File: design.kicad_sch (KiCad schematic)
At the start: 13 parts

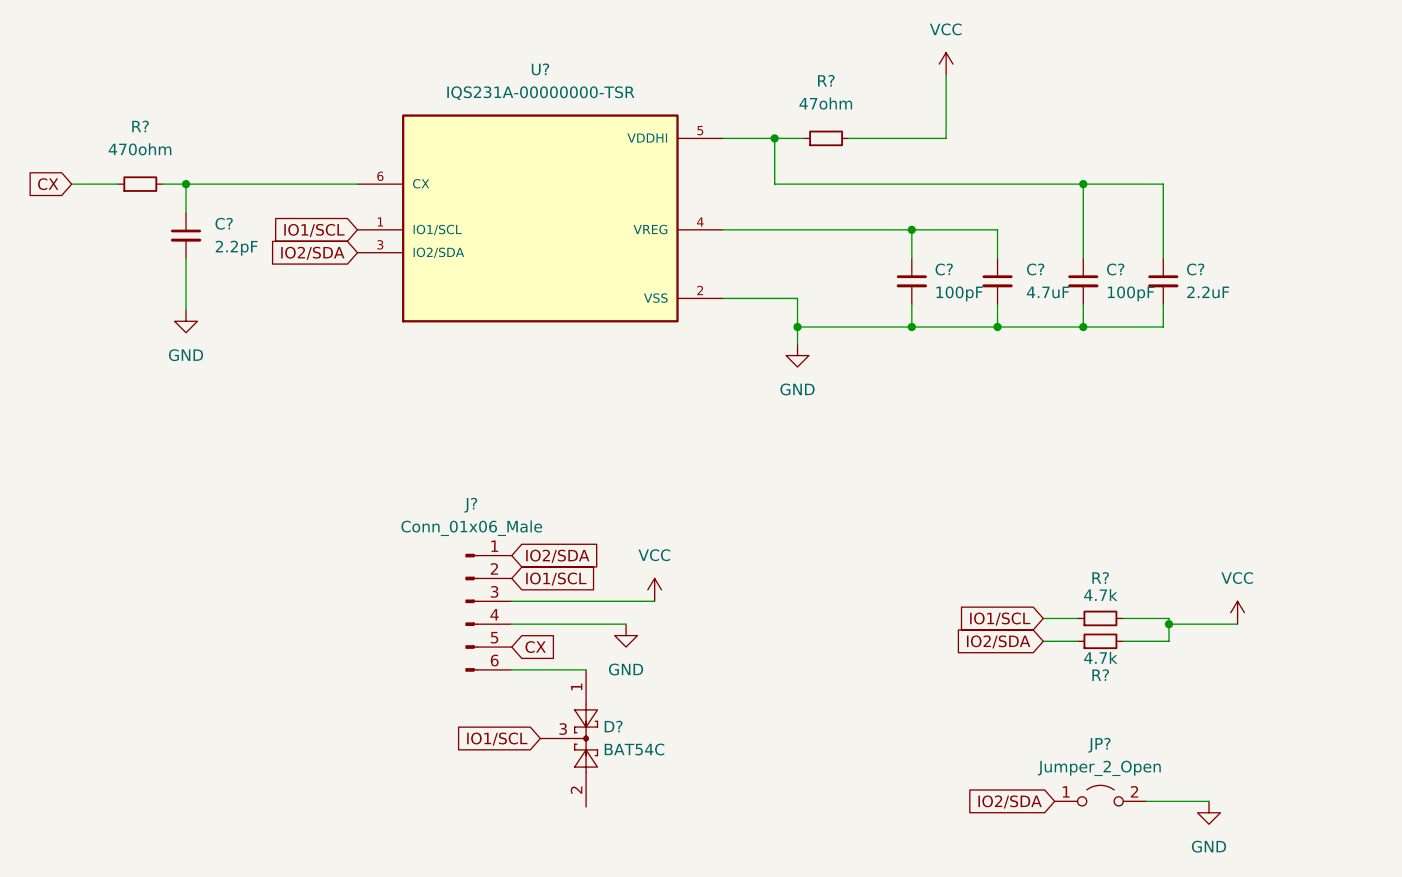
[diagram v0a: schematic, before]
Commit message: annotate and assign footprints
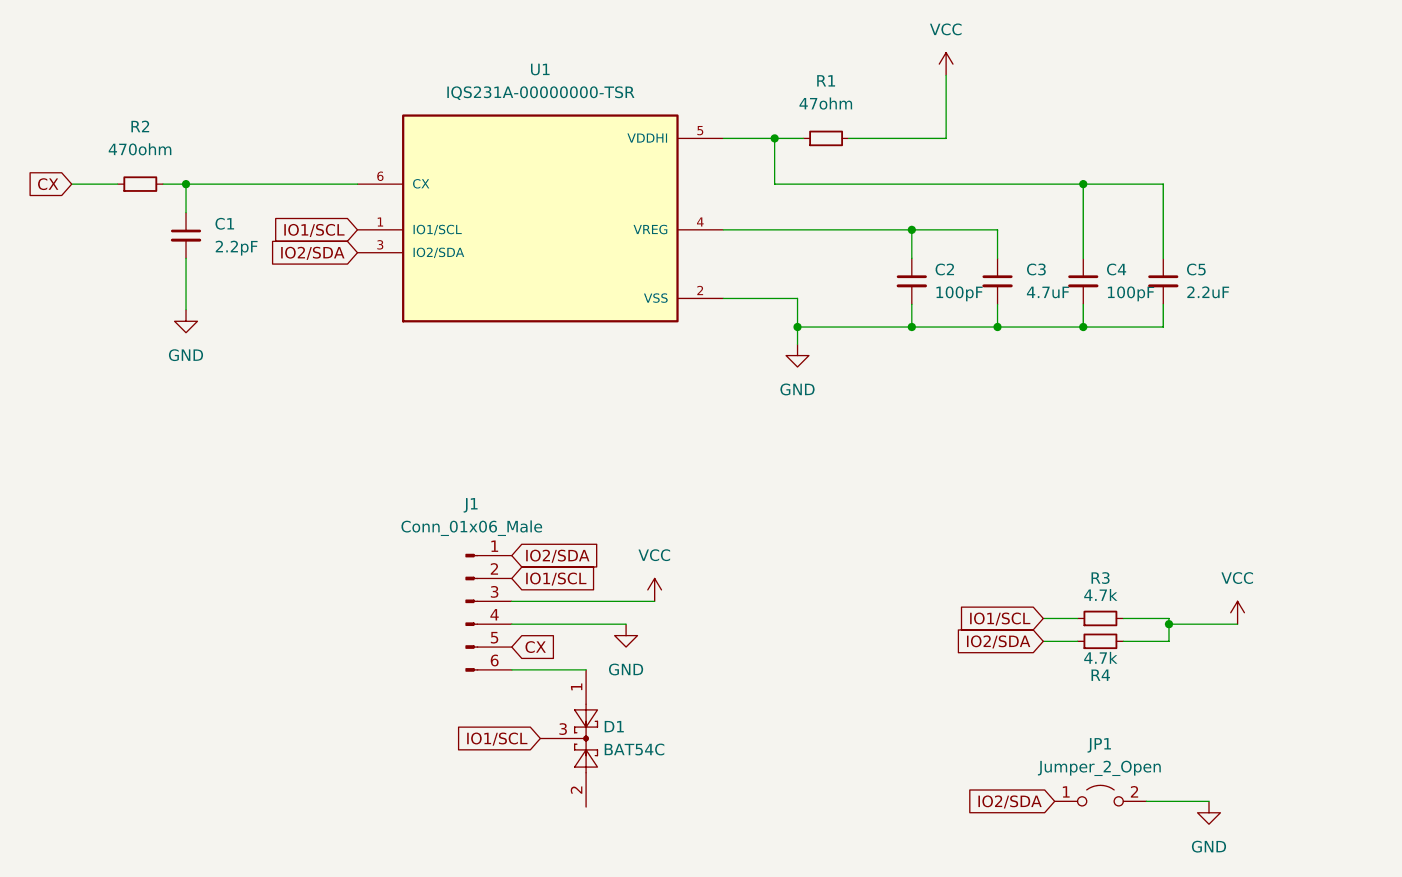
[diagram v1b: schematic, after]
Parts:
- C1, C2, C3, C4, C5: renamed from C?; footprint (none) -> Capacitor_SMD:C_0805_2012Metric
- J1: renamed from J?; footprint (none) -> Connector_PinHeader_2.54mm:PinHeader_1x06_P2.54mm_Vertical
- JP1: renamed from JP?; footprint (none) -> TestPoint:TestPoint_Bridge_Pitch2.54mm_Drill1.0mm
- R1, R2, R3, R4: renamed from R?; footprint (none) -> Resistor_SMD:R_0805_2012Metric
- gave numbers to parts that had none: 2

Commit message: footprint assigned correction
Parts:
- U1: footprint IQS231A-00000000-TSR:SOT95P280X100-6N -> Sensor_Touch_custom:SOT95P280X100-6N
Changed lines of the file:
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@@
     (property "Reference" "U1" (id 0) (at 147.955 66.04 0))
     (property "Value" "IQS231A-00000000-TSR" (id 1) (at 147.955 68.58 0))
-    (property "Footprint" "IQS231A-00000000-TSR:SOT95P280X100-6N" (id 2) (at 147.955 81.28 0)
+    (property "Footprint" "Sensor_Touch_custom:SOT95P280X100-6N" (id 2) (at 147.955 81.28 0)
       (effects (font (size 1.27 1.27)) (justify bottom) hide)
     )
@@
     )
     (path "/21269fcb-7287-4e55-91c9-34cf82a47837"
-      (reference "U1") (unit 1) (value "IQS231A-00000000-TSR") (footprint "IQS231A-00000000-TSR:SOT95P280X100-6N")
-    )
-  )
+      (reference "U1") (unit 1) (value "IQS231A-00000000-TSR") (footprint "Sensor_Touch_custom:SOT95P280X100-6N")
+    )
+  )

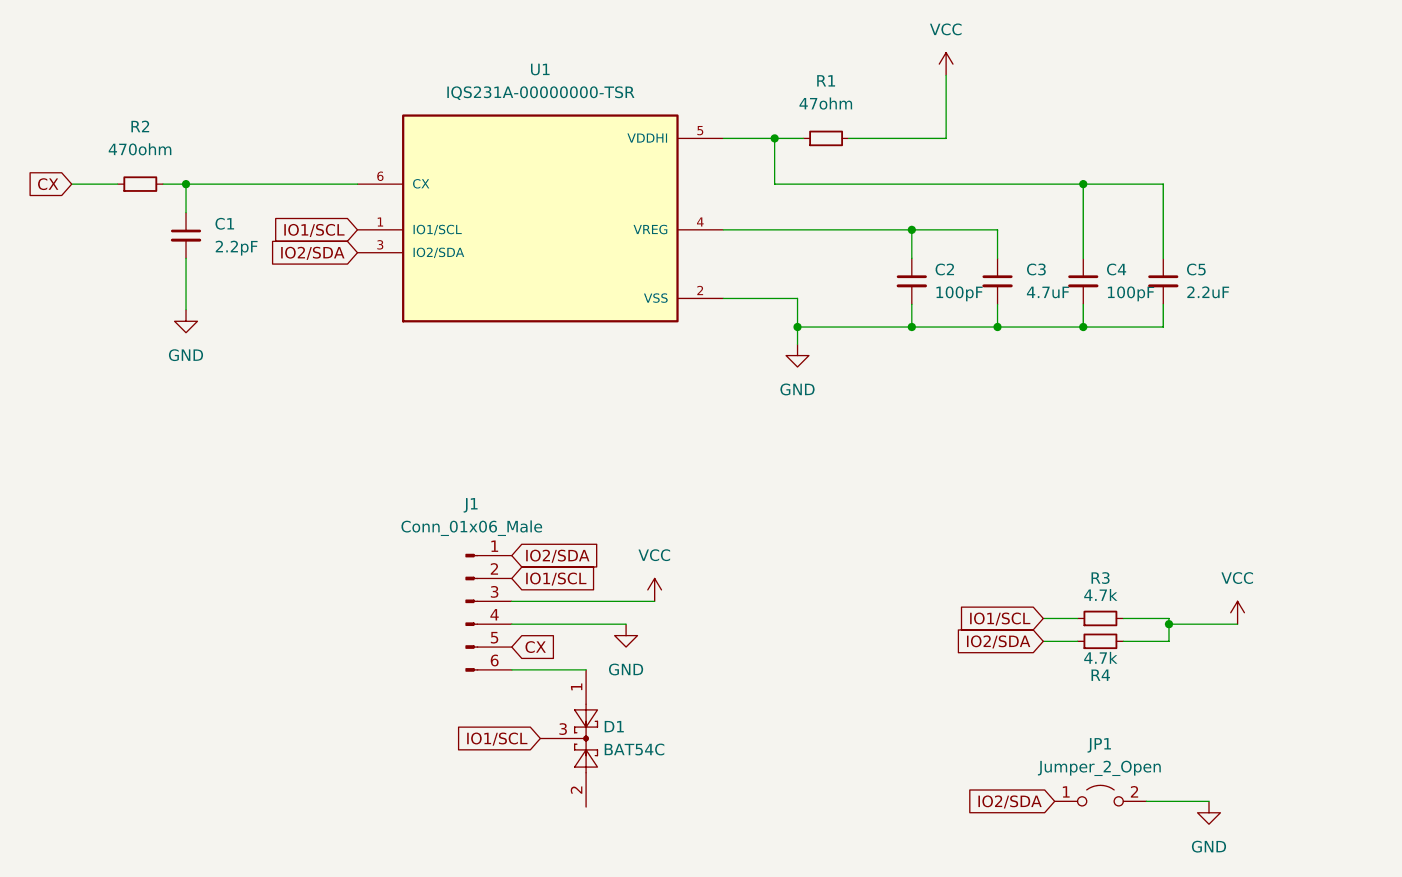
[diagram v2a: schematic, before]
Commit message: pcb layout small sch changes for pcb
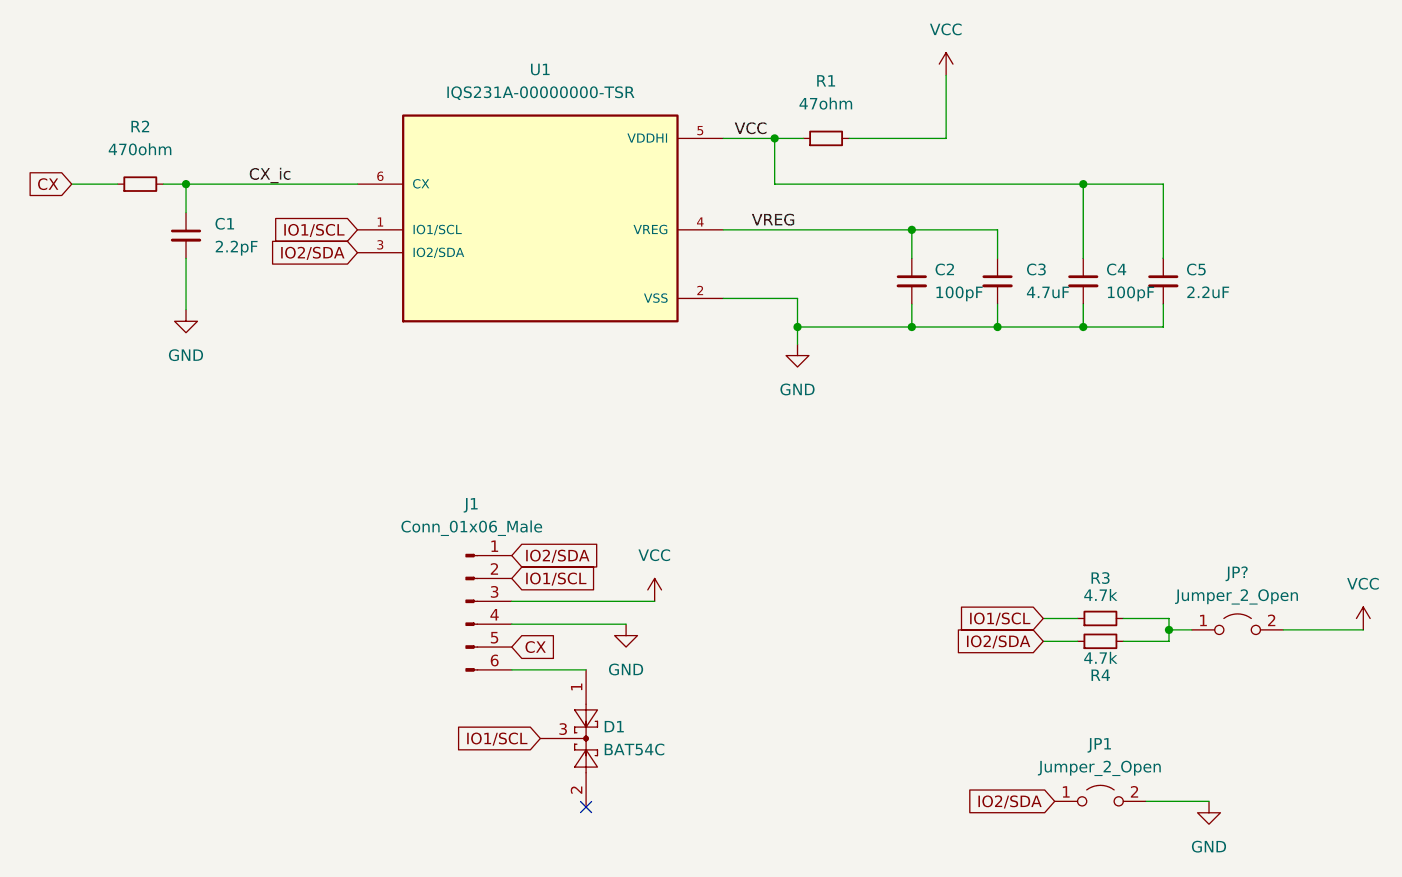
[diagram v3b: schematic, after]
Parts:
- added JP?: Jumper_2_Open, Connector_PinHeader_2.54mm:PinHeader_1x02_P2.54mm_Vertical, symbol Jumper:Jumper_2_Open
- JP1: footprint TestPoint:TestPoint_Bridge_Pitch2.54mm_Drill1.0mm -> Connector_PinHeader_2.54mm:PinHeader_1x02_P2.54mm_Vertical
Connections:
- net VCC: now also C4.1, C5.1, R1.1, U1.5 (VDDHI), JP?.2 (B); no longer R3.2, R4.2
- net VREG: now reaches C2.1, C3.1, U1.4 (VREG)
- net CX_ic: now reaches C1.1, R2.2, U1.6 (CX)
- new net: JP?.1 (A), R3.2, R4.2
- no-connect marks 0 -> 1
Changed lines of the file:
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@@
   (junction (at 189.23 83.82) (diameter 0) (color 0 0 0 0)
   )
-  (junction (at 217.805 127.635) (diameter 0) (color 0 0 0 0)
-  )
   (junction (at 198.755 94.615) (diameter 0) (color 0 0 0 0)
   )
@@
   (junction (at 176.53 94.615) (diameter 0) (color 0 0 0 0)
   )
-  (wire (pts (xy 217.805 127.635) (xy 217.805 127))
+  (junction (at 217.805 128.27) (diameter 0) (color 0 0 0 0)
+  )
+  (no_connect (at 153.035 147.955))
+  (wire (pts (xy 217.805 127) (xy 217.805 128.27))
     (stroke (width 0) (type default) (color 0 0 0 0))
   )
@@
     (stroke (width 0) (type default) (color 0 0 0 0))
   )
-  (wire (pts (xy 217.805 129.54) (xy 217.805 127.635))
-    (stroke (width 0) (type default) (color 0 0 0 0))
-  )
   (wire (pts (xy 144.78 125.095) (xy 160.655 125.095))
     (stroke (width 0) (type default) (color 0 0 0 0))
@@
     (stroke (width 0) (type default) (color 0 0 0 0))
   )
-  (wire (pts (xy 217.805 127.635) (xy 225.425 127.635))
-    (stroke (width 0) (type default) (color 0 0 0 0))
-  )
   (wire (pts (xy 144.78 132.715) (xy 153.035 132.715))
     (stroke (width 0) (type default) (color 0 0 0 0))
   )
+  (wire (pts (xy 217.805 128.27) (xy 220.345 128.27))
+    (stroke (width 0) (type default) (color 0 0 0 0))
+  )
   (wire (pts (xy 173.99 73.66) (xy 177.165 73.66))
     (stroke (width 0) (type default) (color 0 0 0 0))
@@
     (stroke (width 0) (type default) (color 0 0 0 0))
   )
+  (wire (pts (xy 217.805 128.27) (xy 217.805 129.54))
+    (stroke (width 0) (type default) (color 0 0 0 0))
+  )
+  (wire (pts (xy 230.505 128.27) (xy 239.395 128.27))
+    (stroke (width 0) (type default) (color 0 0 0 0))
+  )
   (wire (pts (xy 208.28 94.615) (xy 198.755 94.615))
     (stroke (width 0) (type default) (color 0 0 0 0))
@@
   (wire (pts (xy 217.17 92.075) (xy 217.17 94.615))
     (stroke (width 0) (type default) (color 0 0 0 0))
+  )
+  (label "VCC" (at 169.545 73.66 0)
+    (effects (font (size 1.27 1.27)) (justify left bottom))
+  )
+  (label "VREG" (at 171.45 83.82 0)
+    (effects (font (size 1.27 1.27)) (justify left bottom))
+  )
+  (label "CX_ic" (at 115.57 78.74 0)
+    (effects (font (size 1.27 1.27)) (justify left bottom))
   )
   (global_label "CX" (shape input) (at 95.885 78.74 180) (fields_autoplaced)
@@
     )
     (pin "1")
+  )
+  (symbol (lib_id "Jumper:Jumper_2_Open") (at 225.425 128.27 0) (unit 1)
+    (in_bom yes) (on_board yes) (fields_autoplaced)
+    (property "Reference" "JP?" (id 0) (at 225.425 121.92 0))
+    (property "Value" "Jumper_2_Open" (id 1) (at 225.425 124.46 0))
+    (property "Footprint" "Connector_PinHeader_2.54mm:PinHeader_1x02_P2.54mm_Vertical" (id 2) (at 225.425 128.27 0)
+      (effects (font (size 1.27 1.27)) hide)
+    )
+    (property "Datasheet" "~" (id 3) (at 225.425 128.27 0)
+      (effects (font (size 1.27 1.27)) hide)
+    )
+    (pin "1")
+    (pin "2")
   )
   (symbol (lib_id "Device:C_Small") (at 208.28 89.535 0) (unit 1)
@@
     (pin "1")
   )
-  (symbol (lib_id "power:VCC") (at 225.425 127.635 0) (unit 1)
-    (in_bom yes) (on_board yes) (fields_autoplaced)
-    (property "Reference" "#PWR0104" (id 0) (at 225.425 131.445 0)
-      (effects (font (size 1.27 1.27)) hide)
-    )
-    (property "Value" "VCC" (id 1) (at 225.425 122.555 0))
-    (property "Footprint" "" (id 2) (at 225.425 127.635 0)
-      (effects (font (size 1.27 1.27)) hide)
-    )
-    (property "Datasheet" "" (id 3) (at 225.425 127.635 0)
+  (symbol (lib_id "power:VCC") (at 239.395 128.27 0) (unit 1)
+    (in_bom yes) (on_board yes) (fields_autoplaced)
+    (property "Reference" "#PWR0104" (id 0) (at 239.395 132.08 0)
+      (effects (font (size 1.27 1.27)) hide)
+    )
+    (property "Value" "VCC" (id 1) (at 239.395 123.19 0))
+    (property "Footprint" "" (id 2) (at 239.395 128.27 0)
+      (effects (font (size 1.27 1.27)) hide)
+    )
+    (property "Datasheet" "" (id 3) (at 239.395 128.27 0)
       (effects (font (size 1.27 1.27)) hide)
     )
@@
     (property "Reference" "JP1" (id 0) (at 210.185 140.97 0))
     (property "Value" "Jumper_2_Open" (id 1) (at 210.185 143.51 0))
-    (property "Footprint" "TestPoint:TestPoint_Bridge_Pitch2.54mm_Drill1.0mm" (id 2) (at 210.185 147.32 0)
+    (property "Footprint" "Connector_PinHeader_2.54mm:PinHeader_1x02_P2.54mm_Vertical" (id 2) (at 210.185 147.32 0)
       (effects (font (size 1.27 1.27)) hide)
     )
@@
     )
     (path "/eabaa8d1-3db3-4e54-862d-1cbfc0990697"
-      (reference "JP1") (unit 1) (value "Jumper_2_Open") (footprint "TestPoint:TestPoint_Bridge_Pitch2.54mm_Drill1.0mm")
+      (reference "JP1") (unit 1) (value "Jumper_2_Open") (footprint "Connector_PinHeader_2.54mm:PinHeader_1x02_P2.54mm_Vertical")
+    )
+    (path "/7e065482-e9cb-4feb-8a5e-8a895d9ca9d6"
+      (reference "JP?") (unit 1) (value "Jumper_2_Open") (footprint "Connector_PinHeader_2.54mm:PinHeader_1x02_P2.54mm_Vertical")
     )
     (path "/1ee4c7b2-34da-493e-abfd-70692e4ef9ad"
